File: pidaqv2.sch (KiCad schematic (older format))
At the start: 10 parts, among them J101 Screw_Terminal_01x10, J102 Screw_Terminal_01x06, J103 Conn_01x02_Male, J104 Screw_Terminal_01x04, J105 Screw_Terminal_01x08

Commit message: placed digital gnd plane
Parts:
- removed NT?: Net-Tie_2, symbol Device:Net-Tie_2
- added NT?: Net-Tie_2, symbol Device:Net-Tie_2
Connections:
- wire segments 81 -> 82
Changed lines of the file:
@@
 F0 "amplifier" 50
 F1 "amplifier.sch" 50
-F2 "A+" I L 1800 3700 50
-F3 "B+" I L 1800 3300 50
-F4 "A-" I L 1800 3600 50
-F5 "B-" I L 1800 3200 50
+F2 "A+" I L 1800 3300 50
+F3 "B+" I L 1800 3600 50
+F4 "A-" I L 1800 3200 50
+F5 "B-" I L 1800 3700 50
 F6 "VEXC" I L 1800 3050 50
 F7 "B" O R 2500 3300 50
@@
 	1    0    0    -1
 $EndComp
-Wire Wire Line
-	1800 3200 1600 3200
-Wire Wire Line
-	1600 3200 1600 3150
 Text Notes 750  4600 0    50   ~ 0
 Load Cell Terminals:\nRED/WHITE/BLACK/GREEN\nhttps://www.transducertechniques.com/wiring-color-code.aspx
@@
 	1050 3050 1800 3050
 Wire Wire Line
-	1050 3150 1600 3150
-Wire Wire Line
 	1050 3250 1250 3250
 Wire Wire Line
 	1250 3250 1250 3850
-Wire Wire Line
-	1050 3350 1600 3350
-Wire Wire Line
-	1600 3350 1600 3300
-Wire Wire Line
-	1600 3300 1800 3300
 Wire Wire Line
 	1050 3450 1600 3450
@@
 Wire Wire Line
 	8550 950  8550 1300
-Wire Wire Line
-	8250 3400 8350 3400
-Wire Wire Line
-	8600 3400 8600 3550
-Connection ~ 8350 3400
-Wire Wire Line
-	8350 3400 8450 3400
-Connection ~ 8450 3400
-Wire Wire Line
-	8450 3400 8600 3400
 $Comp
 L power:GND #PWR0103
 U 1 1 5F6AA8DA
-P 8600 3550
-F 0 "#PWR0103" H 8600 3300 50  0001 C CNN
-F 1 "GND" H 8605 3377 50  0000 C CNN
-F 2 "" H 8600 3550 50  0001 C CNN
-F 3 "" H 8600 3550 50  0001 C CNN
-	1    8600 3550
+P 8200 3500
+F 0 "#PWR0103" H 8200 3250 50  0001 C CNN
+F 1 "GND" H 8205 3327 50  0000 C CNN
+F 2 "" H 8200 3500 50  0001 C CNN
+F 3 "" H 8200 3500 50  0001 C CNN
+	1    8200 3500
 	1    0    0    -1
 $EndComp
@@
 Text GLabel 7850 2800 0    50   Output ~ 0
 MOSI
+Text GLabel 7650 2500 0    50   Output ~ 0
+~CS0
 Text GLabel 7650 2650 0    50   Output ~ 0
-~CS0
-Text GLabel 7650 2500 0    50   Output ~ 0
 ~CS1
 Wire Wire Line
@@
 	2950 6550 2850 6550
 NoConn ~ 2850 6550
+Wire Wire Line
+	8250 3400 8250 3500
+Wire Wire Line
+	8250 3500 8200 3500
+Wire Wire Line
+	8350 3400 8450 3400
+$Comp
+L power:GNDREF #PWR0138
+U 1 1 5F7D69C3
+P 8550 3500
+F 0 "#PWR0138" H 8550 3250 50  0001 C CNN
+F 1 "GNDREF" H 8555 3327 50  0000 C CNN
+F 2 "" H 8550 3500 50  0001 C CNN
+F 3 "" H 8550 3500 50  0001 C CNN
+	1    8550 3500
+	1    0    0    -1
+$EndComp
+Wire Wire Line
+	8450 3400 8550 3400
+Wire Wire Line
+	8550 3400 8550 3500
+Connection ~ 8450 3400
+Wire Wire Line
+	1600 3300 1800 3300
+Wire Wire Line
+	1600 3350 1600 3300
+Wire Wire Line
+	1050 3350 1600 3350
+Wire Wire Line
+	1050 3150 1600 3150
+Wire Wire Line
+	1600 3200 1600 3150
+Wire Wire Line
+	1800 3200 1600 3200
 $Comp
 L Device:Net-Tie_2 NT?
-U 1 1 5F799F68
-P 8250 6100
-F 0 "NT?" H 8250 6281 50  0000 C CNN
-F 1 "Net-Tie_2" H 8250 6190 50  0000 C CNN
-F 2 "" H 8250 6100 50  0001 C CNN
-F 3 "~" H 8250 6100 50  0001 C CNN
-	1    8250 6100
-	1    0    0    -1
-$EndComp
-Wire Wire Line
-	8050 6150 8050 6100
-Wire Wire Line
-	8050 6100 8150 6100
-Wire Wire Line
-	8350 6100 8450 6100
-Wire Wire Line
-	8450 6100 8450 6150
+U 1 1 5F800E7F
+P 8250 6050
+F 0 "NT?" H 8250 6231 50  0000 C CNN
+F 1 "Net-Tie_2" H 8250 6140 50  0000 C CNN
+F 2 "" H 8250 6050 50  0001 C CNN
+F 3 "~" H 8250 6050 50  0001 C CNN
+	1    8250 6050
+	1    0    0    -1
+$EndComp
+Wire Wire Line
+	8050 6050 8150 6050
+Wire Wire Line
+	8050 6050 8050 6150
+Wire Wire Line
+	8350 6050 8450 6050
+Wire Wire Line
+	8450 6050 8450 6150
 $EndSCHEMATC

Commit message: temporarily complete
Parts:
- removed NT?: Net-Tie_2, symbol Device:Net-Tie_2
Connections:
- wire segments 82 -> 88
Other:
- moved on the sheet: J104
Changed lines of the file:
@@
 2.5V
 Wire Wire Line
-	3350 1550 2950 1550
+	-1150 1000 -1150 450
 Wire Wire Line
-	2950 1550 2950 1000
+	-750 1100 -1200 1100
 Wire Wire Line
-	3350 1650 2900 1650
+	-1200 1100 -1200 550
 Wire Wire Line
-	2900 1650 2900 1100
-Wire Wire Line
-	3350 1750 2850 1750
-Wire Wire Line
-	3350 1850 2800 1850
+	-750 1200 -1250 1200
 Wire Wire Line
 	3350 1950 2750 1950
 Wire Wire Line
-	2750 1950 2750 1650
+	-1350 1600 -1350 1300
 Wire Wire Line
 	2750 1650 1750 1650
@@
 L Connector:Screw_Terminal_01x04 J104
 U 1 1 5F7080E0
-P 1550 1100
-F 0 "J104" H 1468 1417 50  0000 C CNN
-F 1 "Screw_Terminal_01x04" H 1468 1326 50  0000 C CNN
-F 2 "TerminalBlock_TE-Connectivity:TerminalBlock_TE_282834-4_1x04_P2.54mm_Horizontal" H 1550 1100 50  0001 C CNN
-F 3 "~" H 1550 1100 50  0001 C CNN
-	1    1550 1100
+P 1500 1100
+F 0 "J104" H 1418 1417 50  0000 C CNN
+F 1 "Screw_Terminal_01x04" H 1418 1326 50  0000 C CNN
+F 2 "TerminalBlock_TE-Connectivity:TerminalBlock_TE_282834-4_1x04_P2.54mm_Horizontal" H 1500 1100 50  0001 C CNN
+F 3 "~" H 1500 1100 50  0001 C CNN
+	1    1500 1100
 	-1   0    0    -1
 $EndComp
 Wire Wire Line
-	2800 1300 1750 1300
+	-1300 750  -1300 1300
 Wire Wire Line
-	2800 1300 2800 1850
-Wire Wire Line
-	1750 1200 2850 1200
-Wire Wire Line
-	2850 1200 2850 1750
-Wire Wire Line
-	1750 1100 2900 1100
-Wire Wire Line
-	1750 1000 2950 1000
+	-1250 650  -1250 1200
 Text Notes 1150 1200 2    50   ~ 0
 Extra terminals
@@
 Wire Wire Line
 	1800 3200 1600 3200
-$Comp
-L Device:Net-Tie_2 NT?
-U 1 1 5F800E7F
-P 8250 6050
-F 0 "NT?" H 8250 6231 50  0000 C CNN
-F 1 "Net-Tie_2" H 8250 6140 50  0000 C CNN
-F 2 "" H 8250 6050 50  0001 C CNN
-F 3 "~" H 8250 6050 50  0001 C CNN
-	1    8250 6050
-	1    0    0    -1
-$EndComp
-Wire Wire Line
-	8050 6050 8150 6050
 Wire Wire Line
 	8050 6050 8050 6150
 Wire Wire Line
-	8350 6050 8450 6050
+	8450 6050 8450 6150
+Text GLabel 3350 2450 0    50   Output ~ 0
+2.5V
 Wire Wire Line
-	8450 6050 8450 6150
+	2750 1650 2750 1950
+Wire Wire Line
+	8050 6050 8450 6050
+Wire Wire Line
+	3350 1550 3000 1550
+Wire Wire Line
+	3000 1550 3000 1000
+Wire Wire Line
+	1700 1000 3000 1000
+Wire Wire Line
+	2950 1100 2950 1650
+Wire Wire Line
+	2950 1650 3350 1650
+Wire Wire Line
+	1700 1100 2950 1100
+Wire Wire Line
+	3350 1750 2900 1750
+Wire Wire Line
+	2900 1750 2900 1200
+Wire Wire Line
+	1700 1200 2900 1200
+Wire Wire Line
+	2850 1300 2850 1850
+Wire Wire Line
+	2850 1850 3350 1850
+Wire Wire Line
+	1700 1300 2850 1300
 $EndSCHEMATC

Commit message: set up for reviewers
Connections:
- wire segments 88 -> 81
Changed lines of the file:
@@
 L Connector:Screw_Terminal_01x06 J102
 U 1 1 5F721BF5
-P 850 3350
-F 0 "J102" H 768 2825 50  0000 C CNN
-F 1 "Screw_Terminal_01x06" H 768 2916 50  0000 C CNN
-F 2 "TerminalBlock_TE-Connectivity:TerminalBlock_TE_282834-6_1x06_P2.54mm_Horizontal" H 850 3350 50  0001 C CNN
-F 3 "~" H 850 3350 50  0001 C CNN
-	1    850  3350
-	-1   0    0    1
+P 850 3250
+F 0 "J102" H 768 2725 50  0000 C CNN
+F 1 "Screw_Terminal_01x06" H 768 2816 50  0000 C CNN
+F 2 "TerminalBlock_TE-Connectivity:TerminalBlock_TE_282834-6_1x06_P2.54mm_Horizontal" H 850 3250 50  0001 C CNN
+F 3 "~" H 850 3250 50  0001 C CNN
+	1    850  3250
+	-1   0    0    -1
 $EndComp
 Wire Wire Line
@@
 2.5V
 Wire Wire Line
-	-1150 1000 -1150 450
-Wire Wire Line
-	-750 1100 -1200 1100
-Wire Wire Line
-	-1200 1100 -1200 550
-Wire Wire Line
-	-750 1200 -1250 1200
-Wire Wire Line
 	3350 1950 2750 1950
-Wire Wire Line
-	-1350 1600 -1350 1300
 Wire Wire Line
 	2750 1650 1750 1650
@@
 	-1   0    0    -1
 $EndComp
-Wire Wire Line
-	-1300 750  -1300 1300
-Wire Wire Line
-	-1250 650  -1250 1200
 Text Notes 1150 1200 2    50   ~ 0
 Extra terminals

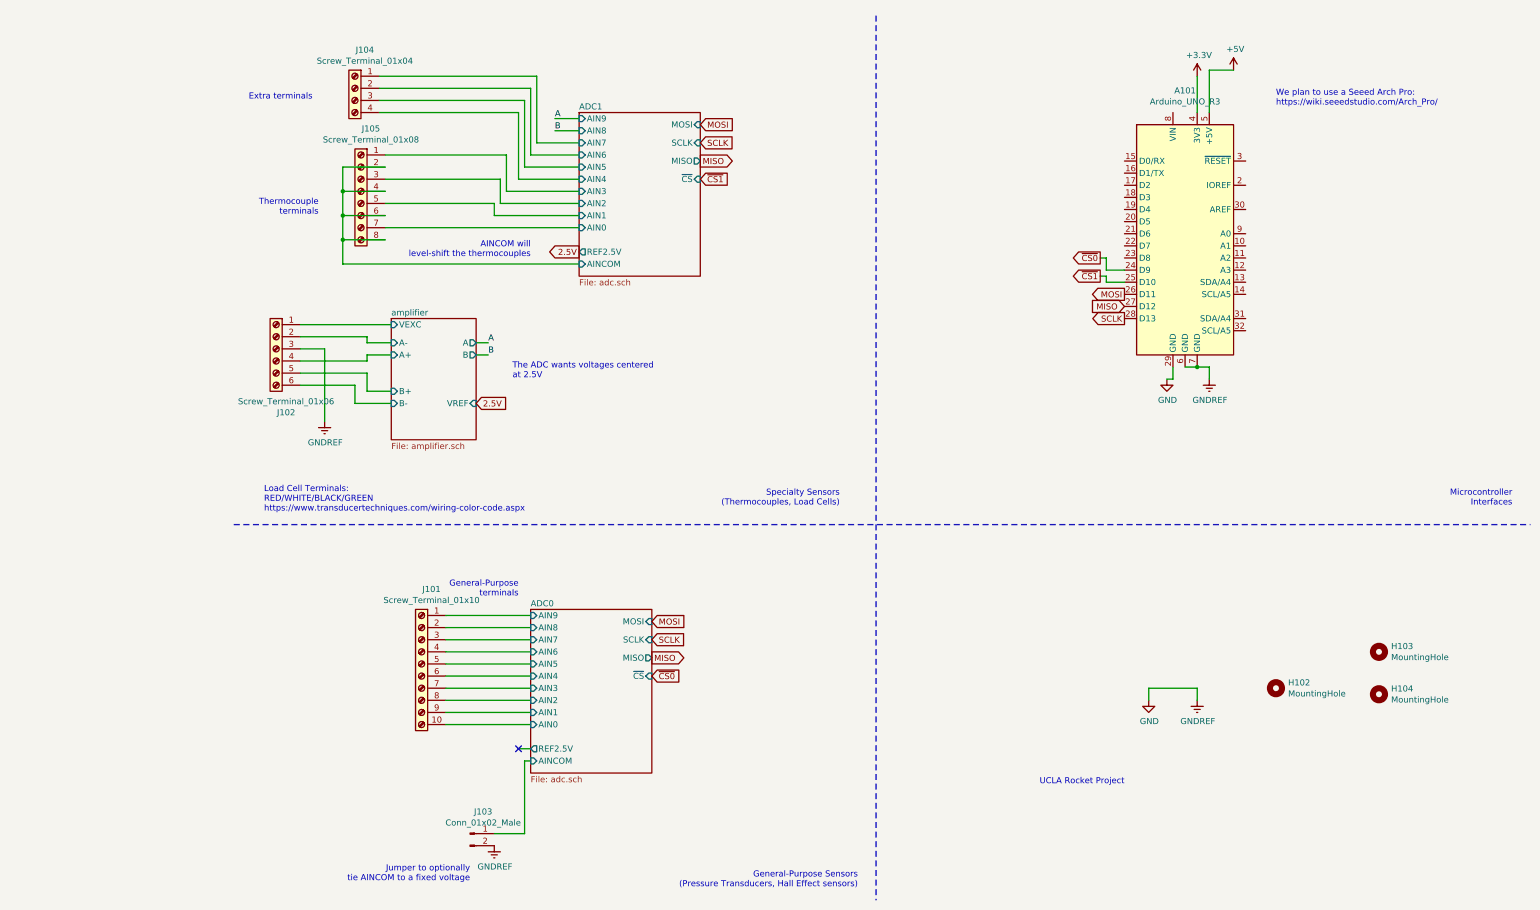
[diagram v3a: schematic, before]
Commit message: Switched out arduino for raspberry pi
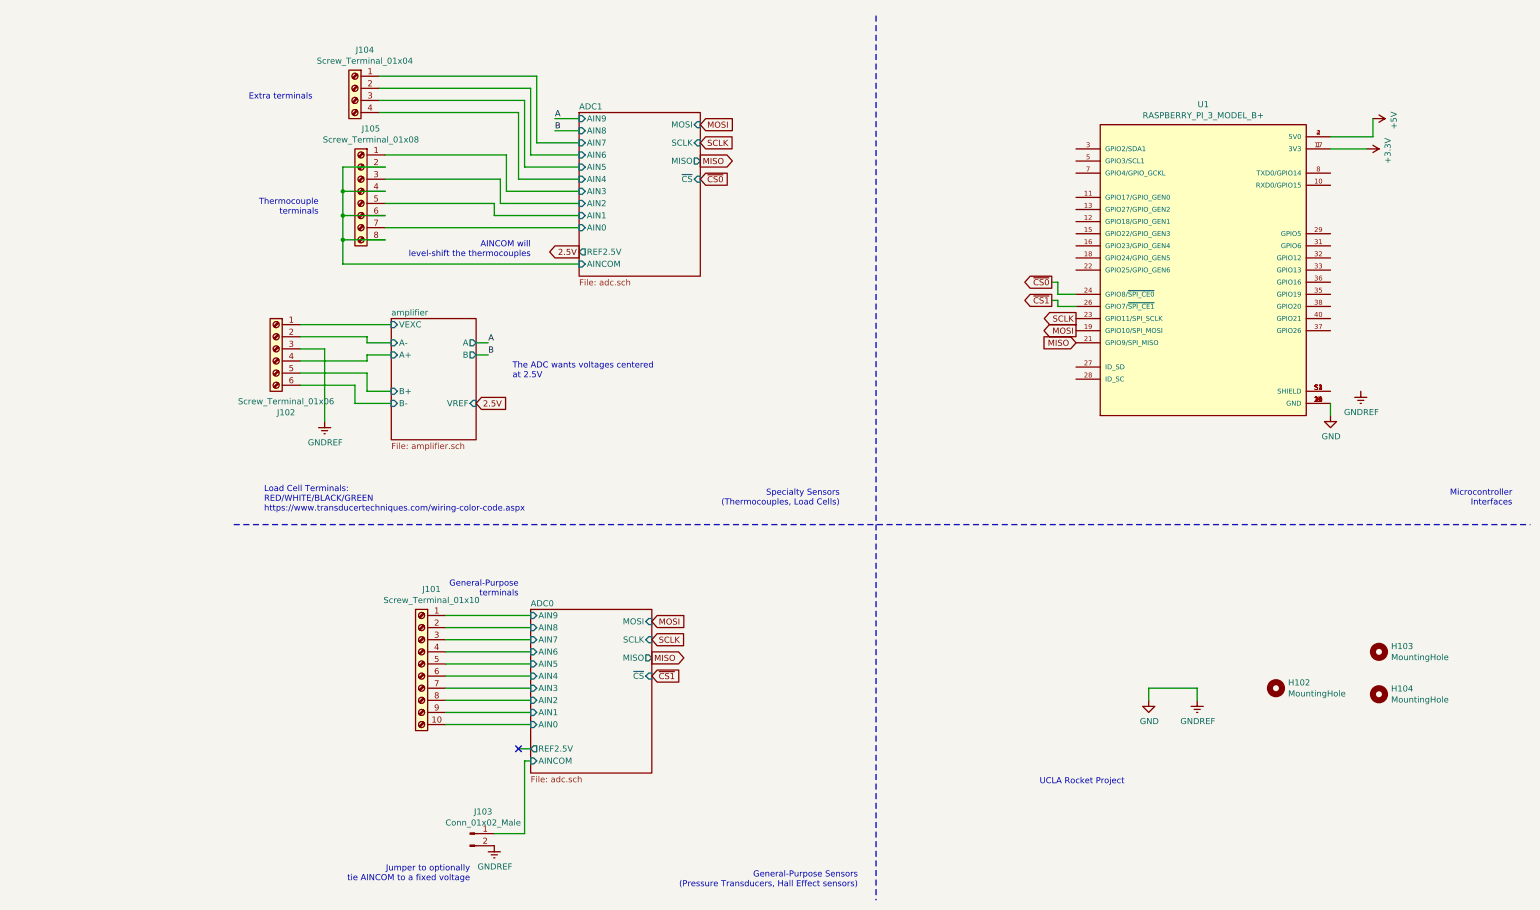
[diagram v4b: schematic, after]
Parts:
- removed A101: Arduino_UNO_R3, Module:Arduino_UNO_R3, symbol MCU_Module:Arduino_UNO_R3
- added U1: RASPBERRY_PI_3_MODEL_B+, MODULE_RASPBERRY_PI_3_MODEL_B+, symbol RASPBERRY_PI_3_MODEL_B_:RASPBERRY_PI_3_MODEL_B+
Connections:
- net +3V3: now also U1.1 (3V3), U1.17 (3V3)
- net +5V: now also U1.2 (5V0), U1.4 (5V0)
- net GND: now also U1.14 (GND), U1.20 (GND), U1.25 (GND), U1.30 (GND), U1.34 (GND), U1.39 (GND), U1.6 (GND), U1.9 (GND)
- net MISO: now also U1.21 (GPIO9/SPI_MISO)
- net MOSI: now also U1.19 (GPIO10/SPI_MOSI)
- net SCLK: now also U1.23 (GPIO11/SPI_SCLK)
- net ~CS0: now also U1.24 (GPIO8/~SPI_CE0~)
- net ~CS1: now also U1.26 (GPIO7/~SPI_CE1~)
- new net: U1.S1 (SHIELD), U1.S2 (SHIELD), U1.S3 (SHIELD), U1.S4 (SHIELD)
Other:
- note removed: "We plan to use a Seeed Arch Pro:\nhttps://wiki.seeedstudio.com/Arch_Pro/"
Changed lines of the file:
@@
 MISO
 Text GLabel 3950 5950 2    50   Input ~ 0
-~CS0
+~CS1
 Text GLabel 4350 1400 2    50   Input ~ 0
 MOSI
@@
 MISO
 Text GLabel 4350 1850 2    50   Input ~ 0
-~CS1
+~CS0
 $Sheet
 S 3350 1300 1000 1350
@@
 	1500 3700 1800 3700
 $Comp
-L MCU_Module:Arduino_UNO_R3 A101
-U 1 1 5F69BB4E
-P 8350 2300
-F 0 "A101" H 8350 3481 50  0000 C CNN
-F 1 "Arduino_UNO_R3" H 8350 3390 50  0000 C CNN
-F 2 "Module:Arduino_UNO_R3" H 8350 2300 50  0001 C CIN
-F 3 "https://www.arduino.cc/en/Main/arduinoBoardUno" H 8350 2300 50  0001 C CNN
-	1    8350 2300
-	1    0    0    -1
-$EndComp
-$Comp
 L power:+3.3V #PWR0101
 U 1 1 5F6A340B
-P 8450 1000
-F 0 "#PWR0101" H 8450 850 50  0001 C CNN
-F 1 "+3.3V" H 8465 1173 50  0000 C CNN
-F 2 "" H 8450 1000 50  0001 C CNN
-F 3 "" H 8450 1000 50  0001 C CNN
-	1    8450 1000
-	1    0    0    -1
-$EndComp
-Wire Wire Line
-	8450 1300 8450 1000
-$Comp
-L power:+5V #PWR0102
-U 1 1 5F6A5CF8
-P 8750 950
-F 0 "#PWR0102" H 8750 800 50  0001 C CNN
-F 1 "+5V" H 8765 1123 50  0000 C CNN
-F 2 "" H 8750 950 50  0001 C CNN
-F 3 "" H 8750 950 50  0001 C CNN
-	1    8750 950
-	1    0    0    -1
-$EndComp
-Wire Wire Line
-	8750 950  8550 950
-Wire Wire Line
-	8550 950  8550 1300
+P 9850 1600
+F 0 "#PWR0101" H 9850 1450 50  0001 C CNN
+F 1 "+3.3V" H 9865 1773 50  0000 C CNN
+F 2 "" H 9850 1600 50  0001 C CNN
+F 3 "" H 9850 1600 50  0001 C CNN
+	1    9850 1600
+	0    1    1    0
+$EndComp
+Wire Wire Line
+	9550 1600 9850 1600
 $Comp
 L power:GND #PWR0103
 U 1 1 5F6AA8DA
-P 8200 3500
-F 0 "#PWR0103" H 8200 3250 50  0001 C CNN
-F 1 "GND" H 8205 3327 50  0000 C CNN
-F 2 "" H 8200 3500 50  0001 C CNN
-F 3 "" H 8200 3500 50  0001 C CNN
-	1    8200 3500
-	1    0    0    -1
-$EndComp
-Text GLabel 7850 3000 0    50   Output ~ 0
+P 9550 3800
+F 0 "#PWR0103" H 9550 3550 50  0001 C CNN
+F 1 "GND" H 9555 3627 50  0000 C CNN
+F 2 "" H 9550 3800 50  0001 C CNN
+F 3 "" H 9550 3800 50  0001 C CNN
+	1    9550 3800
+	1    0    0    -1
+$EndComp
+Text GLabel 7450 3000 0    50   Output ~ 0
 SCLK
-Text GLabel 7850 2900 0    50   Input ~ 0
+Text GLabel 7450 3200 0    50   Input ~ 0
 MISO
-Text GLabel 7850 2800 0    50   Output ~ 0
+Text GLabel 7450 3100 0    50   Output ~ 0
 MOSI
-Text GLabel 7650 2500 0    50   Output ~ 0
-~CS0
-Text GLabel 7650 2650 0    50   Output ~ 0
-~CS1
-Wire Wire Line
-	7850 2700 7700 2700
-Wire Wire Line
-	7700 2700 7700 2650
-Wire Wire Line
-	7700 2650 7650 2650
-Wire Wire Line
-	7850 2600 7700 2600
-Wire Wire Line
-	7700 2600 7700 2500
-Wire Wire Line
-	7700 2500 7650 2500
-Text Notes 9100 1250 0    50   ~ 0
-We plan to use a Seeed Arch Pro:\nhttps://wiki.seeedstudio.com/Arch_Pro/
+Wire Wire Line
+	7450 2900 7300 2900
+Wire Wire Line
+	7300 2900 7300 2850
+Wire Wire Line
+	7450 2800 7300 2800
+Wire Wire Line
+	7300 2800 7300 2700
+Wire Wire Line
+	7300 2700 7250 2700
 Wire Wire Line
 	2500 3300 2600 3300
@@
 NoConn ~ 2850 6550
 Wire Wire Line
-	8250 3400 8250 3500
-Wire Wire Line
-	8250 3500 8200 3500
-Wire Wire Line
-	8350 3400 8450 3400
+	9550 3700 9550 3800
 $Comp
 L power:GNDREF #PWR0138
 U 1 1 5F7D69C3
-P 8550 3500
-F 0 "#PWR0138" H 8550 3250 50  0001 C CNN
-F 1 "GNDREF" H 8555 3327 50  0000 C CNN
-F 2 "" H 8550 3500 50  0001 C CNN
-F 3 "" H 8550 3500 50  0001 C CNN
-	1    8550 3500
-	1    0    0    -1
-$EndComp
-Wire Wire Line
-	8450 3400 8550 3400
-Wire Wire Line
-	8550 3400 8550 3500
-Connection ~ 8450 3400
+P 9800 3600
+F 0 "#PWR0138" H 9800 3350 50  0001 C CNN
+F 1 "GNDREF" H 9805 3427 50  0000 C CNN
+F 2 "" H 9800 3600 50  0001 C CNN
+F 3 "" H 9800 3600 50  0001 C CNN
+	1    9800 3600
+	1    0    0    -1
+$EndComp
 Wire Wire Line
 	1600 3300 1800 3300
@@
 Wire Wire Line
 	1700 1300 2850 1300
+$Comp
+L RASPBERRY_PI_3_MODEL_B_:RASPBERRY_PI_3_MODEL_B+ U1
+U 1 1 5FC69FBF
+P 8550 2400
+F 0 "U1" H 8500 3567 50  0000 C CNN
+F 1 "RASPBERRY_PI_3_MODEL_B+" H 8500 3476 50  0000 C CNN
+F 2 "MODULE_RASPBERRY_PI_3_MODEL_B+" H 8550 2400 50  0001 L BNN
+F 3 "" H 8550 2400 50  0001 L BNN
+F 4 "Manufacturer Recommendations" H 8550 2400 50  0001 L BNN "STANDARD"
+F 5 "18mm" H 8550 2400 50  0001 L BNN "MAXIMUM_PACKAGE_HIEGHT"
+F 6 "1.0" H 8550 2400 50  0001 L BNN "PARTREV"
+F 7 "Raspberry Pi" H 8550 2400 50  0001 L BNN "MANUFACTURER"
+	1    8550 2400
+	1    0    0    -1
+$EndComp
+Text GLabel 7250 2700 0    50   Output ~ 0
+~CS0
+Wire Wire Line
+	7300 2850 7250 2850
+Text GLabel 7250 2850 0    50   Output ~ 0
+~CS1
+Wire Wire Line
+	9900 1500 9550 1500
+Wire Wire Line
+	9900 1350 9900 1500
+$Comp
+L power:+5V #PWR0102
+U 1 1 5F6A5CF8
+P 9900 1350
+F 0 "#PWR0102" H 9900 1200 50  0001 C CNN
+F 1 "+5V" H 9915 1523 50  0000 C CNN
+F 2 "" H 9900 1350 50  0001 C CNN
+F 3 "" H 9900 1350 50  0001 C CNN
+	1    9900 1350
+	0    1    1    0
+$EndComp
 $EndSCHEMATC
